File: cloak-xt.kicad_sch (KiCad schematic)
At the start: 23 parts, among them J1 USB_C_Receptacle_USB2.0, J2 Conn_01x20, J3 Conn_01x20, U1 STM32F072CBT6, U2 PRTR5V0U2X

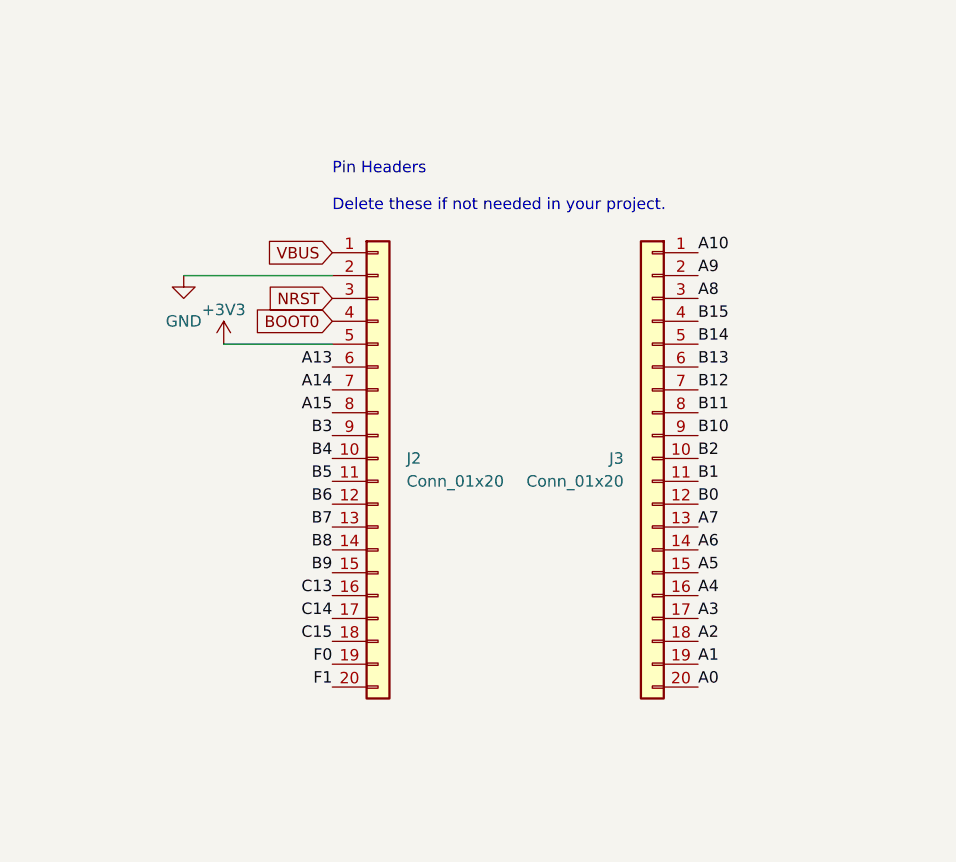
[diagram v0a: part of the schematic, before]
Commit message: Remove pin headers and edge cuts
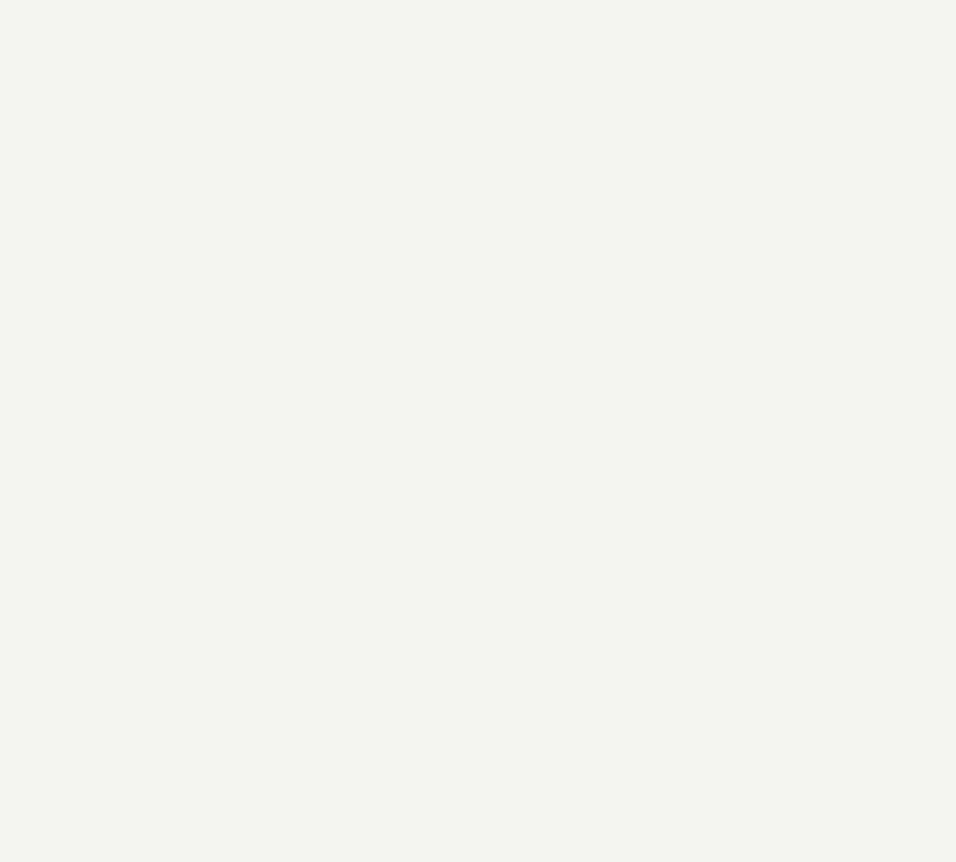
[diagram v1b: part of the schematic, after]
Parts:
- removed J2, J3: Conn_01x20, Connector_PinHeader_2.54mm:PinHeader_1x20_P2.54mm_Vertical, symbol Connector_Generic:Conn_01x20
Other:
- note removed: "Pin Headers Delete these if not needed in your project."
